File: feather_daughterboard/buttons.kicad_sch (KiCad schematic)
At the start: 16 parts

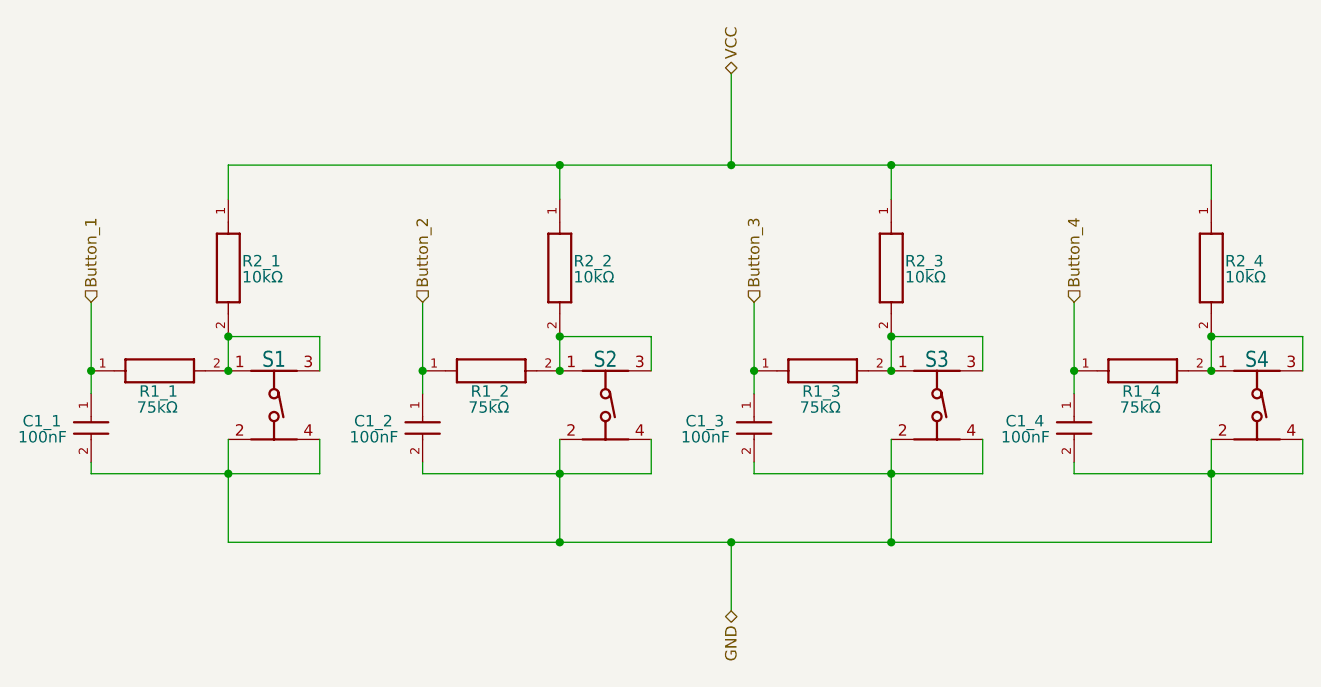
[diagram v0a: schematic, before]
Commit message: changed the connector on the daughter board
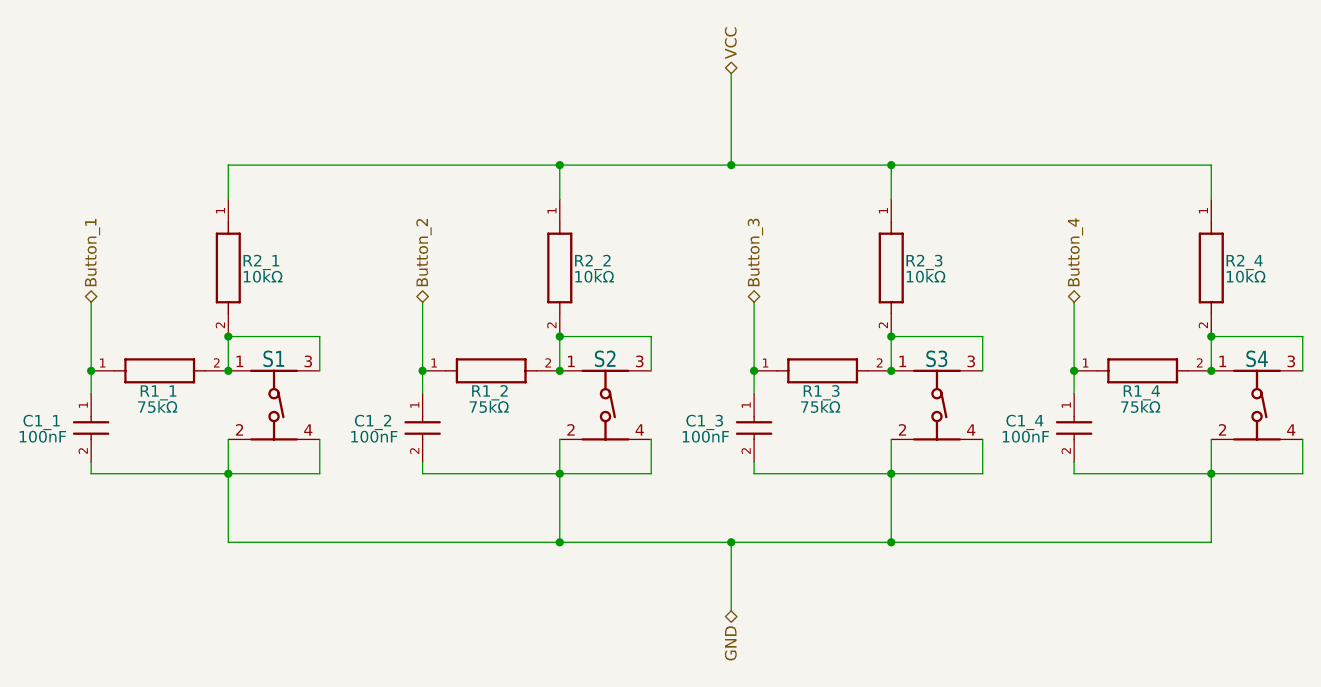
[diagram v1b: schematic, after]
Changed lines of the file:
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@@
 	)
 	(hierarchical_label "Button_2"
-		(shape input)
+		(shape bidirectional)
 		(at 121.92 87.63 90)
 		(fields_autoplaced yes)
@@
 	)
 	(hierarchical_label "Button_3"
-		(shape input)
+		(shape bidirectional)
 		(at 158.75 87.63 90)
 		(fields_autoplaced yes)
@@
 	)
 	(hierarchical_label "Button_4"
-		(shape input)
+		(shape bidirectional)
 		(at 194.31 87.63 90)
 		(fields_autoplaced yes)
@@
 	)
 	(hierarchical_label "Button_1"
-		(shape input)
+		(shape bidirectional)
 		(at 85.09 87.63 90)
 		(fields_autoplaced yes)
